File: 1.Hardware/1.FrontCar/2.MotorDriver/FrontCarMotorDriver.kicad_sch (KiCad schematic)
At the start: 52 parts, among them IC1 DRV8701ERGER, IC2 DRV8701ERGER, IC3 SN74LVC244APW, J1 Conn_02x03_Odd_Even, J2 Conn_01x02, J3 Conn_01x02, J4 Conn_02x03_Odd_Even, J5 Conn_02x03_Odd_Even, M1 Motor_DC, M2 Motor_DC, Q1 NMOS, Q2 NMOS, Q3 NMOS, Q4 NMOS, Q5 NMOS, Q6 NMOS, Q7 NMOS, Q8 NMOS, SW1 SW_SPDT, SW2 SW_SPDT, U1 AMS1117-3.3

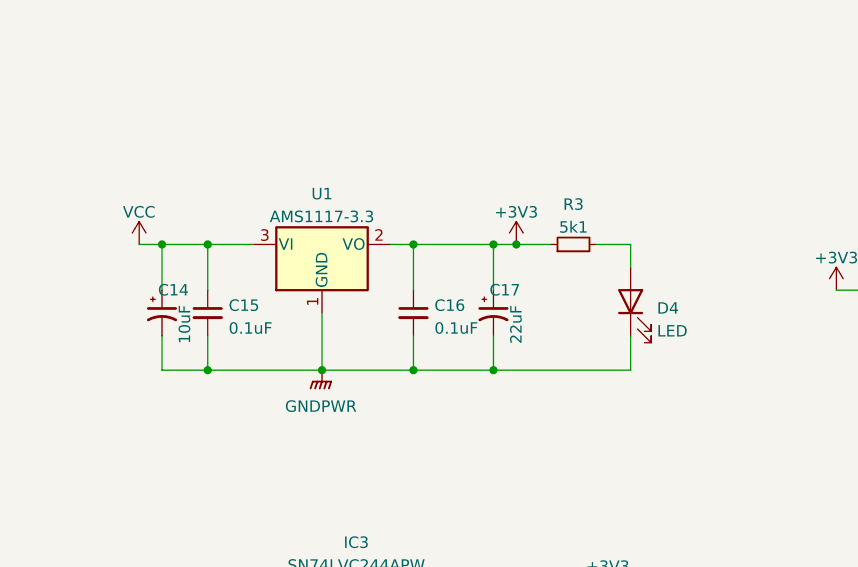
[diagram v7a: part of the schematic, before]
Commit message: 增加两个外接，带按键屏幕模块
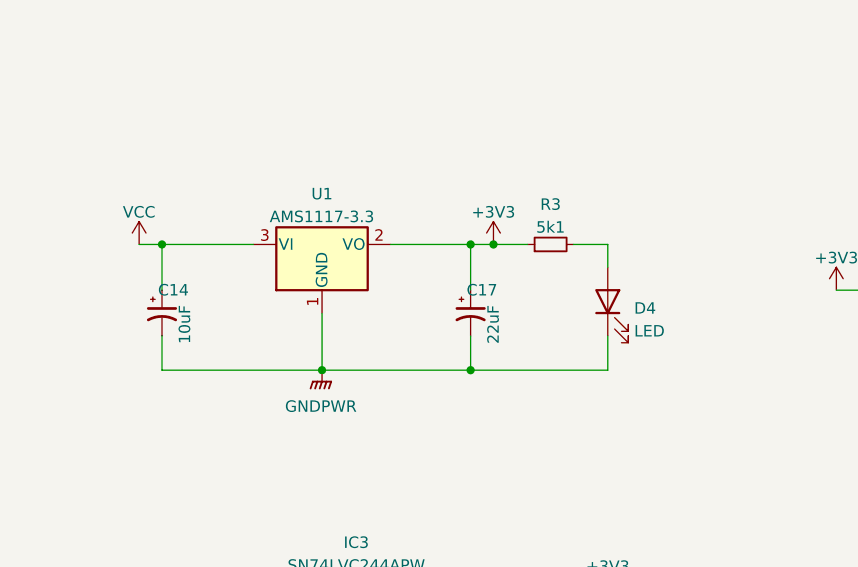
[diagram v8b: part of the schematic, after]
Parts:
- removed C15, C16: 0.1uF, Capacitor_SMD:C_0603_1608Metric, symbol Device:C_Small
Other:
- moved on the sheet: C17, D4, R3
